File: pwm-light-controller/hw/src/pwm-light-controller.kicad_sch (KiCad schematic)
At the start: 13 parts, among them J1 PEAK SWITCH, J2 EXT PEAK, J3 INPUT, J4 OUTPUT, Q1 AO3400A, U1 AMS1117-5.0, U2 ATtiny13A-P

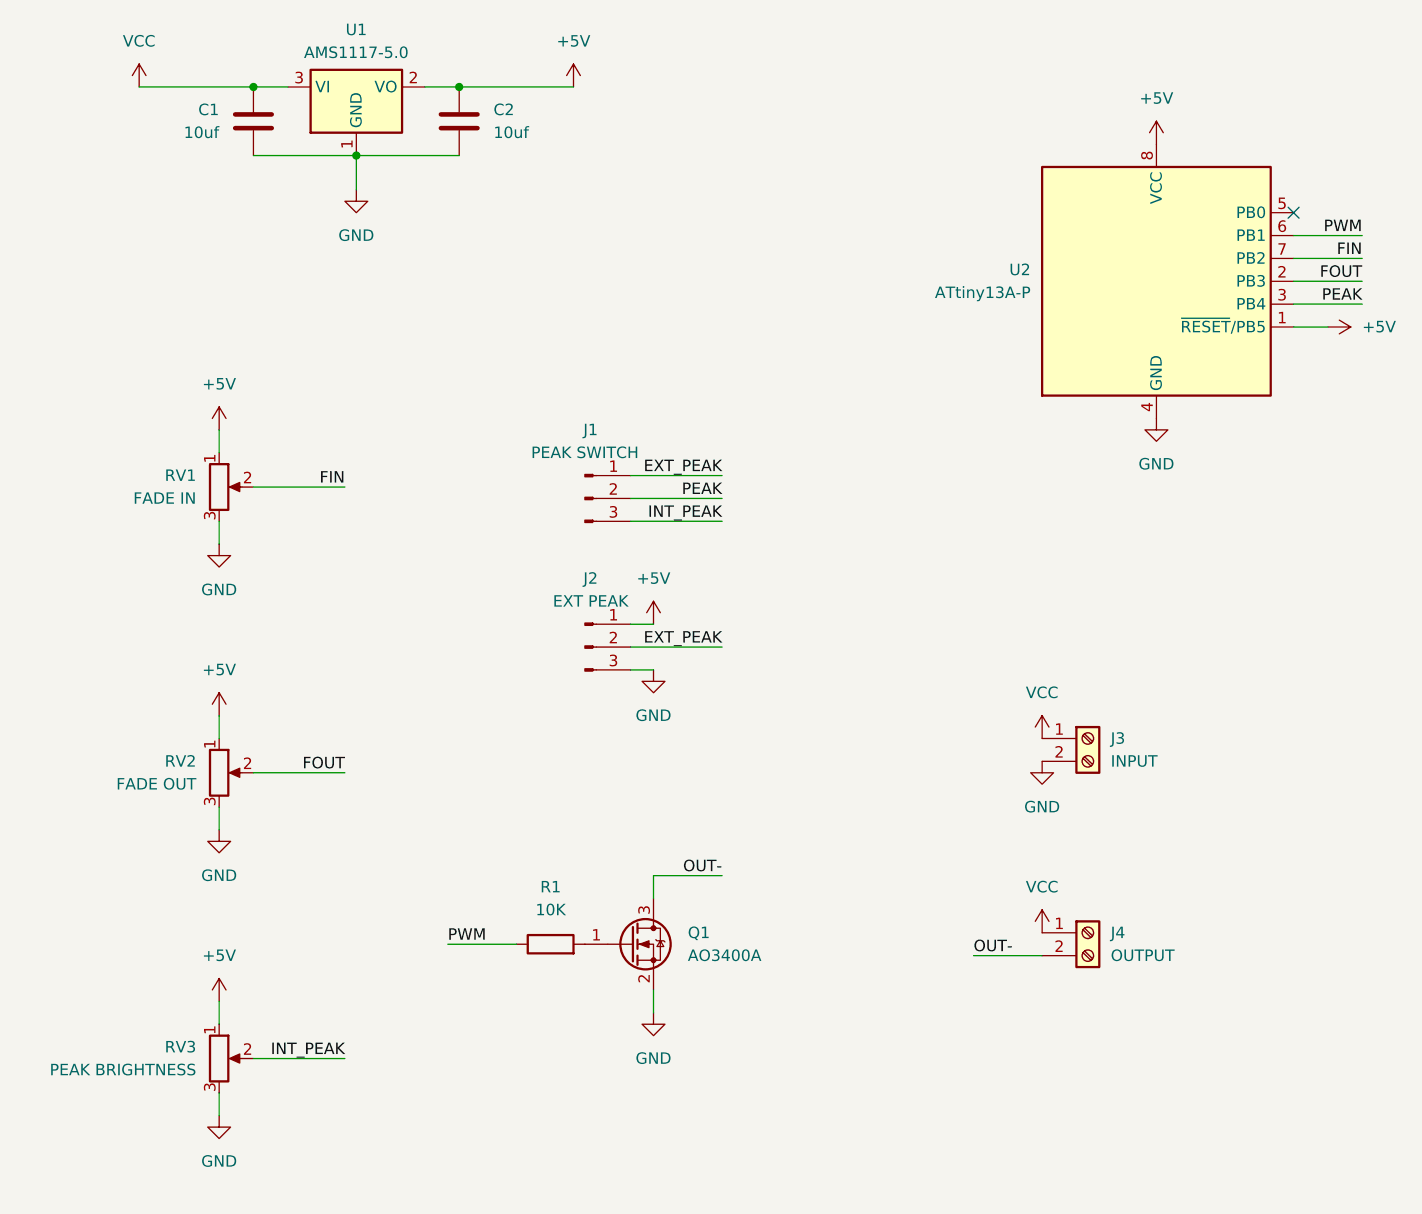
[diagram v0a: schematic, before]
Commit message: Add header for external switch
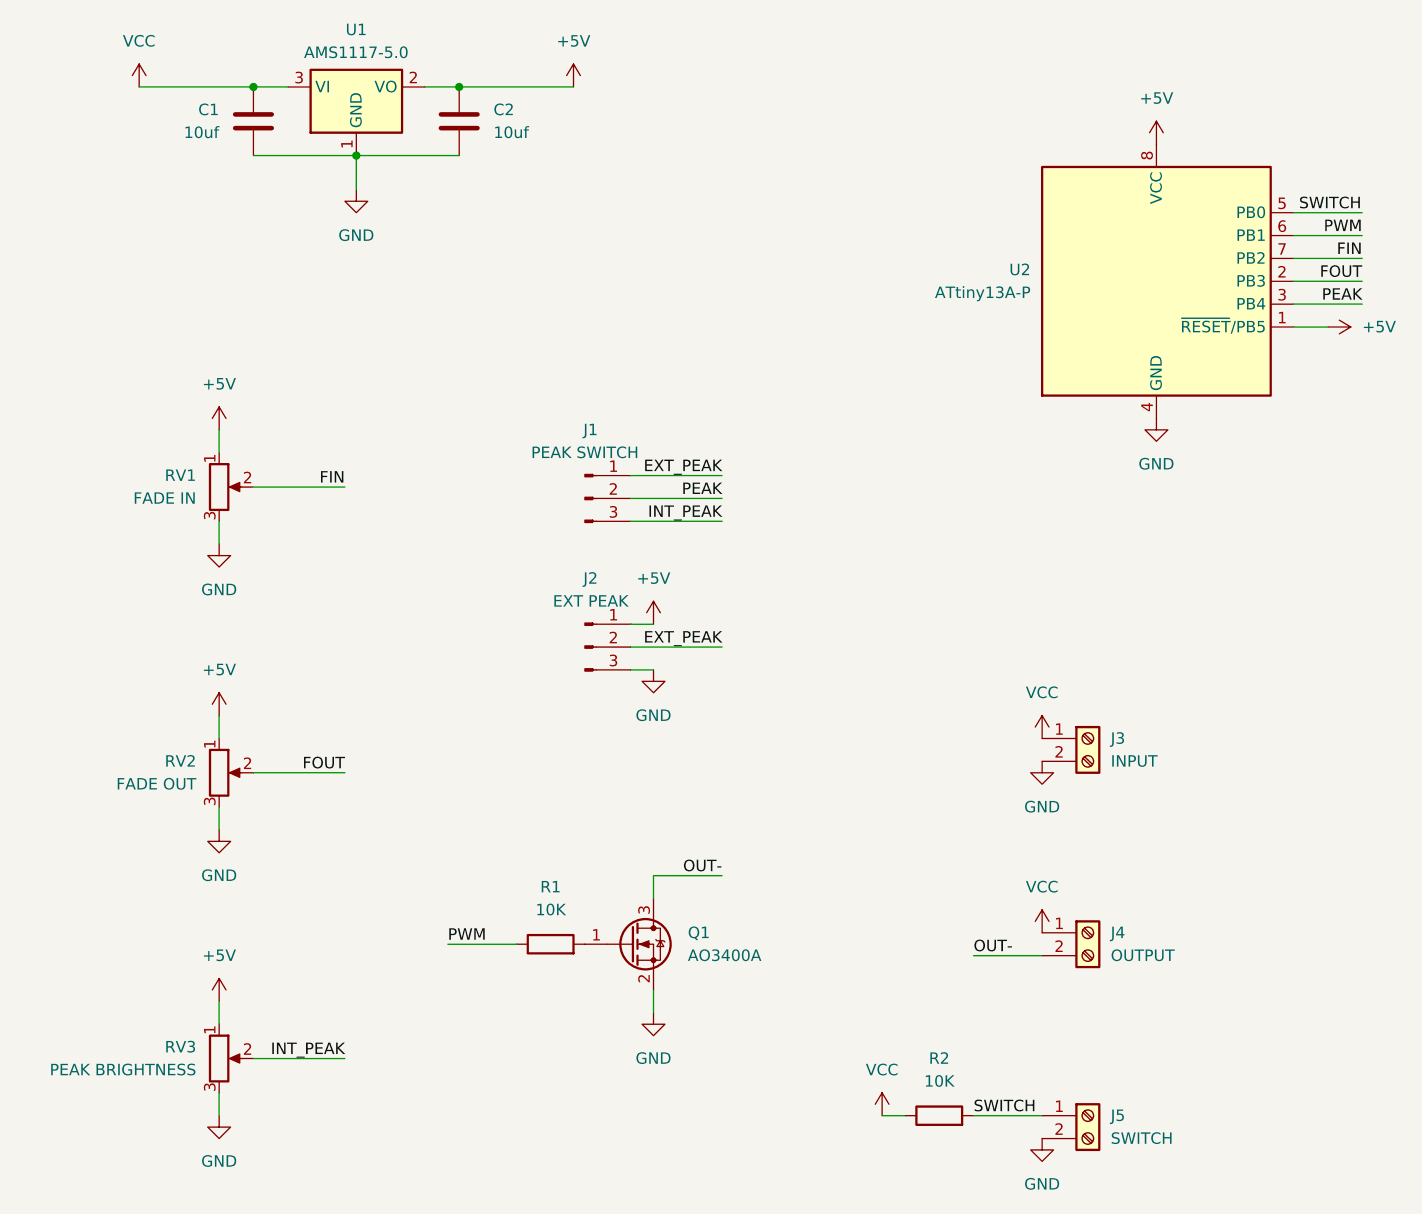
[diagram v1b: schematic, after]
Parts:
- added J5: SWITCH, symbol Connector:Screw_Terminal_01x02
- added R2: 10K, symbol Device:R
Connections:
- net GND: now also J5.2 (Pin_2)
- net VCC: now also R2.1
- net SWITCH: now reaches U2.5 (PB0)
- net SWITCH: now also J5.1 (Pin_1), R2.2
- no-connect marks 1 -> 0
